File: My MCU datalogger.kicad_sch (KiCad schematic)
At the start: 0 parts

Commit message: added resistor
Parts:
- added R?: R, symbol Device:R
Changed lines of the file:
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@@
     (comment 1 "©2022 by P. CARDON")
+  )
+  (symbol (lib_id "Device:R") (at 81.28 44.45 0) (unit 1)
+    (in_bom yes) (on_board yes) (fields_autoplaced)
+    (property "Reference" "R?" (id 0) (at 83.82 43.1799 0)
+      (effects (font (size 1.27 1.27)) (justify left))
+    )
+    (property "Value" "R" (id 1) (at 83.82 45.7199 0)
+      (effects (font (size 1.27 1.27)) (justify left))
+    )
+    (property "Footprint" "" (id 2) (at 79.502 44.45 90)
+      (effects (font (size 1.27 1.27)) hide)
+    )
+    (property "Datasheet" "~" (id 3) (at 81.28 44.45 0)
+      (effects (font (size 1.27 1.27)) hide)
+    )
+    (pin "1")
+    (pin "2")
   )
   (sheet_instances
     (path "/" (page "1"))
   )
+  (symbol_instances
+    (path "/c63b5fc8-661c-44e7-ac4b-00c9fb9e97ae"
+      (reference "R?") (unit 1) (value "R") (footprint "")
+    )
+  )
 )

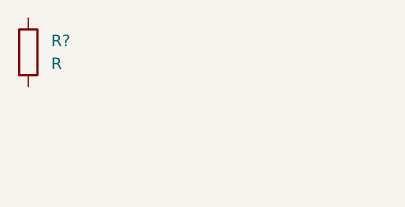
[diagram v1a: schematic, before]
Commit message: added capacitor
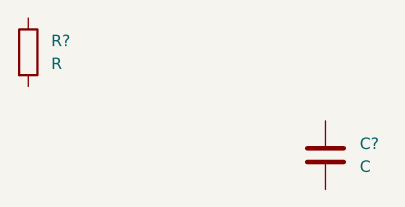
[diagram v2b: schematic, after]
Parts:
- added C?: C, symbol Device:C
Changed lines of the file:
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@@
+    (pin "2")
+  )
+  (symbol (lib_id "Device:C") (at 114.3 55.88 0) (unit 1)
+    (in_bom yes) (on_board yes) (fields_autoplaced)
+    (property "Reference" "C?" (id 0) (at 118.11 54.6099 0)
+      (effects (font (size 1.27 1.27)) (justify left))
+    )
+    (property "Value" "C" (id 1) (at 118.11 57.1499 0)
+      (effects (font (size 1.27 1.27)) (justify left))
+    )
+    (property "Footprint" "" (id 2) (at 115.2652 59.69 0)
+      (effects (font (size 1.27 1.27)) hide)
+    )
+    (property "Datasheet" "~" (id 3) (at 114.3 55.88 0)
+      (effects (font (size 1.27 1.27)) hide)
+    )
+    (pin "1")
     (pin "2")
   )
@@
   )
   (symbol_instances
+    (path "/ed4bd9ec-e796-40ac-a1eb-1a92d42f0ee0"
+      (reference "C?") (unit 1) (value "C") (footprint "")
+    )
     (path "/c63b5fc8-661c-44e7-ac4b-00c9fb9e97ae"
       (reference "R?") (unit 1) (value "R") (footprint "")

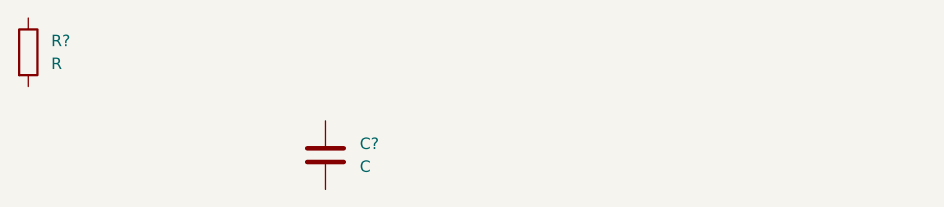
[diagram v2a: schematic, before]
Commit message: testing with new capacitors
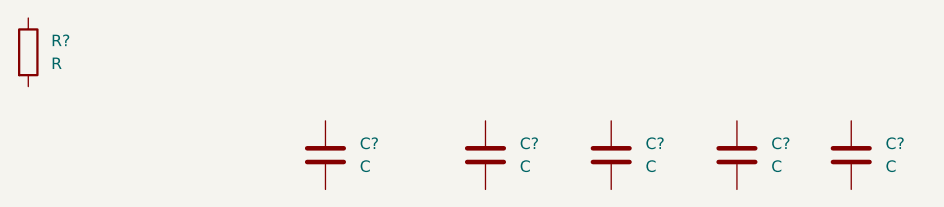
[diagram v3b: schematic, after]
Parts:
- added C? (x4): C, symbol Device:C
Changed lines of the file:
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@@
     (comment 1 "©2022 by P. CARDON")
+  )
+  (symbol (lib_id "Device:C") (at 160.02 55.88 0) (unit 1)
+    (in_bom yes) (on_board yes) (fields_autoplaced)
+    (property "Reference" "C?" (id 0) (at 163.83 54.6099 0)
+      (effects (font (size 1.27 1.27)) (justify left))
+    )
+    (property "Value" "C" (id 1) (at 163.83 57.1499 0)
+      (effects (font (size 1.27 1.27)) (justify left))
+    )
+    (property "Footprint" "" (id 2) (at 160.9852 59.69 0)
+      (effects (font (size 1.27 1.27)) hide)
+    )
+    (property "Datasheet" "~" (id 3) (at 160.02 55.88 0)
+      (effects (font (size 1.27 1.27)) hide)
+    )
+    (pin "1")
+    (pin "2")
+  )
+  (symbol (lib_id "Device:C") (at 172.72 55.88 0) (unit 1)
+    (in_bom yes) (on_board yes) (fields_autoplaced)
+    (property "Reference" "C?" (id 0) (at 176.53 54.6099 0)
+      (effects (font (size 1.27 1.27)) (justify left))
+    )
+    (property "Value" "C" (id 1) (at 176.53 57.1499 0)
+      (effects (font (size 1.27 1.27)) (justify left))
+    )
+    (property "Footprint" "" (id 2) (at 173.6852 59.69 0)
+      (effects (font (size 1.27 1.27)) hide)
+    )
+    (property "Datasheet" "~" (id 3) (at 172.72 55.88 0)
+      (effects (font (size 1.27 1.27)) hide)
+    )
+    (pin "1")
+    (pin "2")
+  )
+  (symbol (lib_id "Device:C") (at 132.08 55.88 0) (unit 1)
+    (in_bom yes) (on_board yes) (fields_autoplaced)
+    (property "Reference" "C?" (id 0) (at 135.89 54.6099 0)
+      (effects (font (size 1.27 1.27)) (justify left))
+    )
+    (property "Value" "C" (id 1) (at 135.89 57.1499 0)
+      (effects (font (size 1.27 1.27)) (justify left))
+    )
+    (property "Footprint" "" (id 2) (at 133.0452 59.69 0)
+      (effects (font (size 1.27 1.27)) hide)
+    )
+    (property "Datasheet" "~" (id 3) (at 132.08 55.88 0)
+      (effects (font (size 1.27 1.27)) hide)
+    )
+    (pin "1")
+    (pin "2")
   )
   (symbol (lib_id "Device:R") (at 81.28 44.45 0) (unit 1)
@@
     )
     (property "Datasheet" "~" (id 3) (at 81.28 44.45 0)
+      (effects (font (size 1.27 1.27)) hide)
+    )
+    (pin "1")
+    (pin "2")
+  )
+  (symbol (lib_id "Device:C") (at 146.05 55.88 0) (unit 1)
+    (in_bom yes) (on_board yes) (fields_autoplaced)
+    (property "Reference" "C?" (id 0) (at 149.86 54.6099 0)
+      (effects (font (size 1.27 1.27)) (justify left))
+    )
+    (property "Value" "C" (id 1) (at 149.86 57.1499 0)
+      (effects (font (size 1.27 1.27)) (justify left))
+    )
+    (property "Footprint" "" (id 2) (at 147.0152 59.69 0)
+      (effects (font (size 1.27 1.27)) hide)
+    )
+    (property "Datasheet" "~" (id 3) (at 146.05 55.88 0)
       (effects (font (size 1.27 1.27)) hide)
     )
@@
   )
   (symbol_instances
+    (path "/371747a2-e35e-43b9-b7ce-a597ed85ad70"
+      (reference "C?") (unit 1) (value "C") (footprint "")
+    )
+    (path "/5cfaff8f-4cb1-4092-acac-68ea8803d576"
+      (reference "C?") (unit 1) (value "C") (footprint "")
+    )
+    (path "/7b9bce85-d170-4751-8f9d-84fa2277030b"
+      (reference "C?") (unit 1) (value "C") (footprint "")
+    )
+    (path "/c6d91237-16c9-4474-8603-2d912175aa18"
+      (reference "C?") (unit 1) (value "C") (footprint "")
+    )
     (path "/ed4bd9ec-e796-40ac-a1eb-1a92d42f0ee0"
       (reference "C?") (unit 1) (value "C") (footprint "")

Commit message: Added annotation
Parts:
- gave numbers to parts that had none: 6
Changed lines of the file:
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@@
   (symbol (lib_id "Device:C") (at 160.02 55.88 0) (unit 1)
     (in_bom yes) (on_board yes) (fields_autoplaced)
-    (property "Reference" "C?" (id 0) (at 163.83 54.6099 0)
+    (property "Reference" "C4" (id 0) (at 163.83 54.6099 0)
       (effects (font (size 1.27 1.27)) (justify left))
     )
@@
   (symbol (lib_id "Device:C") (at 172.72 55.88 0) (unit 1)
     (in_bom yes) (on_board yes) (fields_autoplaced)
-    (property "Reference" "C?" (id 0) (at 176.53 54.6099 0)
+    (property "Reference" "C5" (id 0) (at 176.53 54.6099 0)
       (effects (font (size 1.27 1.27)) (justify left))
     )
@@
   (symbol (lib_id "Device:C") (at 132.08 55.88 0) (unit 1)
     (in_bom yes) (on_board yes) (fields_autoplaced)
-    (property "Reference" "C?" (id 0) (at 135.89 54.6099 0)
+    (property "Reference" "C2" (id 0) (at 135.89 54.6099 0)
       (effects (font (size 1.27 1.27)) (justify left))
     )
@@
   (symbol (lib_id "Device:R") (at 81.28 44.45 0) (unit 1)
     (in_bom yes) (on_board yes) (fields_autoplaced)
-    (property "Reference" "R?" (id 0) (at 83.82 43.1799 0)
+    (property "Reference" "R1" (id 0) (at 83.82 43.1799 0)
       (effects (font (size 1.27 1.27)) (justify left))
     )
@@
   (symbol (lib_id "Device:C") (at 146.05 55.88 0) (unit 1)
     (in_bom yes) (on_board yes) (fields_autoplaced)
-    (property "Reference" "C?" (id 0) (at 149.86 54.6099 0)
+    (property "Reference" "C3" (id 0) (at 149.86 54.6099 0)
       (effects (font (size 1.27 1.27)) (justify left))
     )
@@
   (symbol (lib_id "Device:C") (at 114.3 55.88 0) (unit 1)
     (in_bom yes) (on_board yes) (fields_autoplaced)
-    (property "Reference" "C?" (id 0) (at 118.11 54.6099 0)
+    (property "Reference" "C1" (id 0) (at 118.11 54.6099 0)
       (effects (font (size 1.27 1.27)) (justify left))
     )
@@
   )
   (symbol_instances
+    (path "/ed4bd9ec-e796-40ac-a1eb-1a92d42f0ee0"
+      (reference "C1") (unit 1) (value "C") (footprint "")
+    )
+    (path "/7b9bce85-d170-4751-8f9d-84fa2277030b"
+      (reference "C2") (unit 1) (value "C") (footprint "")
+    )
+    (path "/c6d91237-16c9-4474-8603-2d912175aa18"
+      (reference "C3") (unit 1) (value "C") (footprint "")
+    )
     (path "/371747a2-e35e-43b9-b7ce-a597ed85ad70"
-      (reference "C?") (unit 1) (value "C") (footprint "")
+      (reference "C4") (unit 1) (value "C") (footprint "")
     )
     (path "/5cfaff8f-4cb1-4092-acac-68ea8803d576"
-      (reference "C?") (unit 1) (value "C") (footprint "")
-    )
-    (path "/7b9bce85-d170-4751-8f9d-84fa2277030b"
-      (reference "C?") (unit 1) (value "C") (footprint "")
-    )
-    (path "/c6d91237-16c9-4474-8603-2d912175aa18"
-      (reference "C?") (unit 1) (value "C") (footprint "")
-    )
-    (path "/ed4bd9ec-e796-40ac-a1eb-1a92d42f0ee0"
-      (reference "C?") (unit 1) (value "C") (footprint "")
+      (reference "C5") (unit 1) (value "C") (footprint "")
     )
     (path "/c63b5fc8-661c-44e7-ac4b-00c9fb9e97ae"
-      (reference "R?") (unit 1) (value "R") (footprint "")
+      (reference "R1") (unit 1) (value "R") (footprint "")
     )
   )

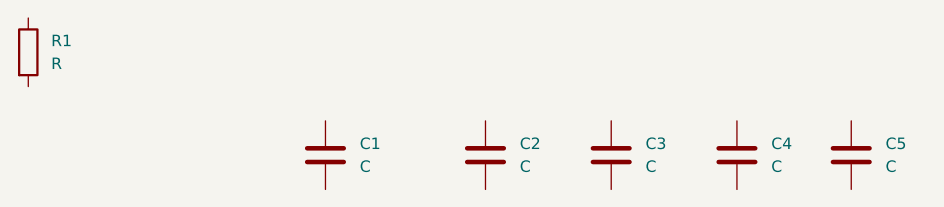
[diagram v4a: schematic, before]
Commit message: Update My MCU datalogger.kicad_sch
Changed C5 to C25
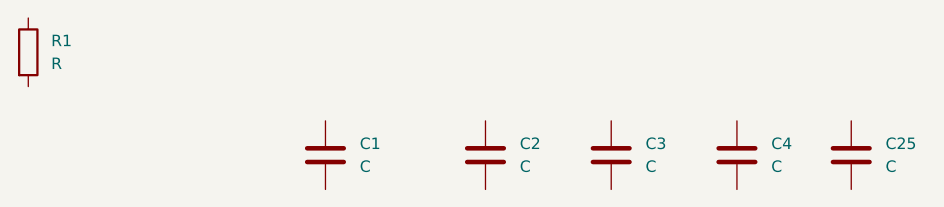
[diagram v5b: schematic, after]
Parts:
- renumbered C5 to C25
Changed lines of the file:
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@@
   (symbol (lib_id "Device:C") (at 172.72 55.88 0) (unit 1)
     (in_bom yes) (on_board yes) (fields_autoplaced)
-    (property "Reference" "C5" (id 0) (at 176.53 54.6099 0)
+    (property "Reference" "C25" (id 0) (at 176.53 54.6099 0)
       (effects (font (size 1.27 1.27)) (justify left))
     )
